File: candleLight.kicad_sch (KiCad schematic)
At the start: 42 parts, among them J1 USB_C_Receptacle_USB2.0, J2 Conn_Phoenix, J3 Conn_SWD, J4 Conn_USART1, J5 Conn_BOOT0, SW1 MST22D18G2 125, U1 STM32F072C8Tx, U2 AMS1117-3.3, U3 TJA1051TK-3, Y1 8MHz

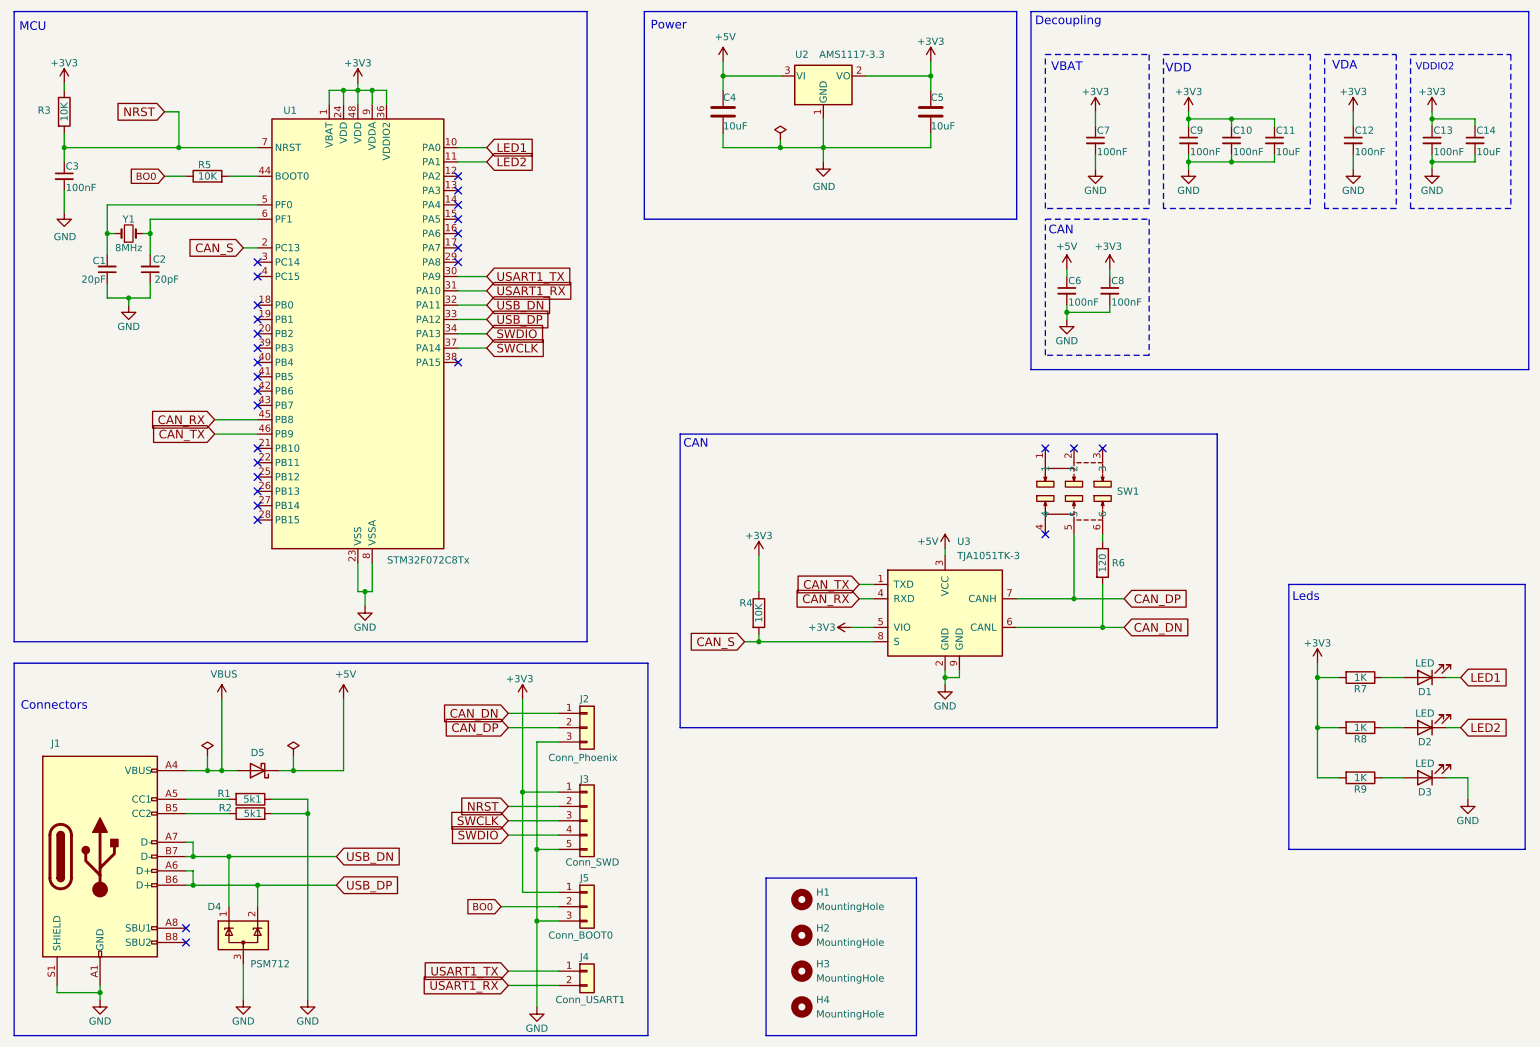
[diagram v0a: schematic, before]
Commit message: uppdate silkscreen and SPI header
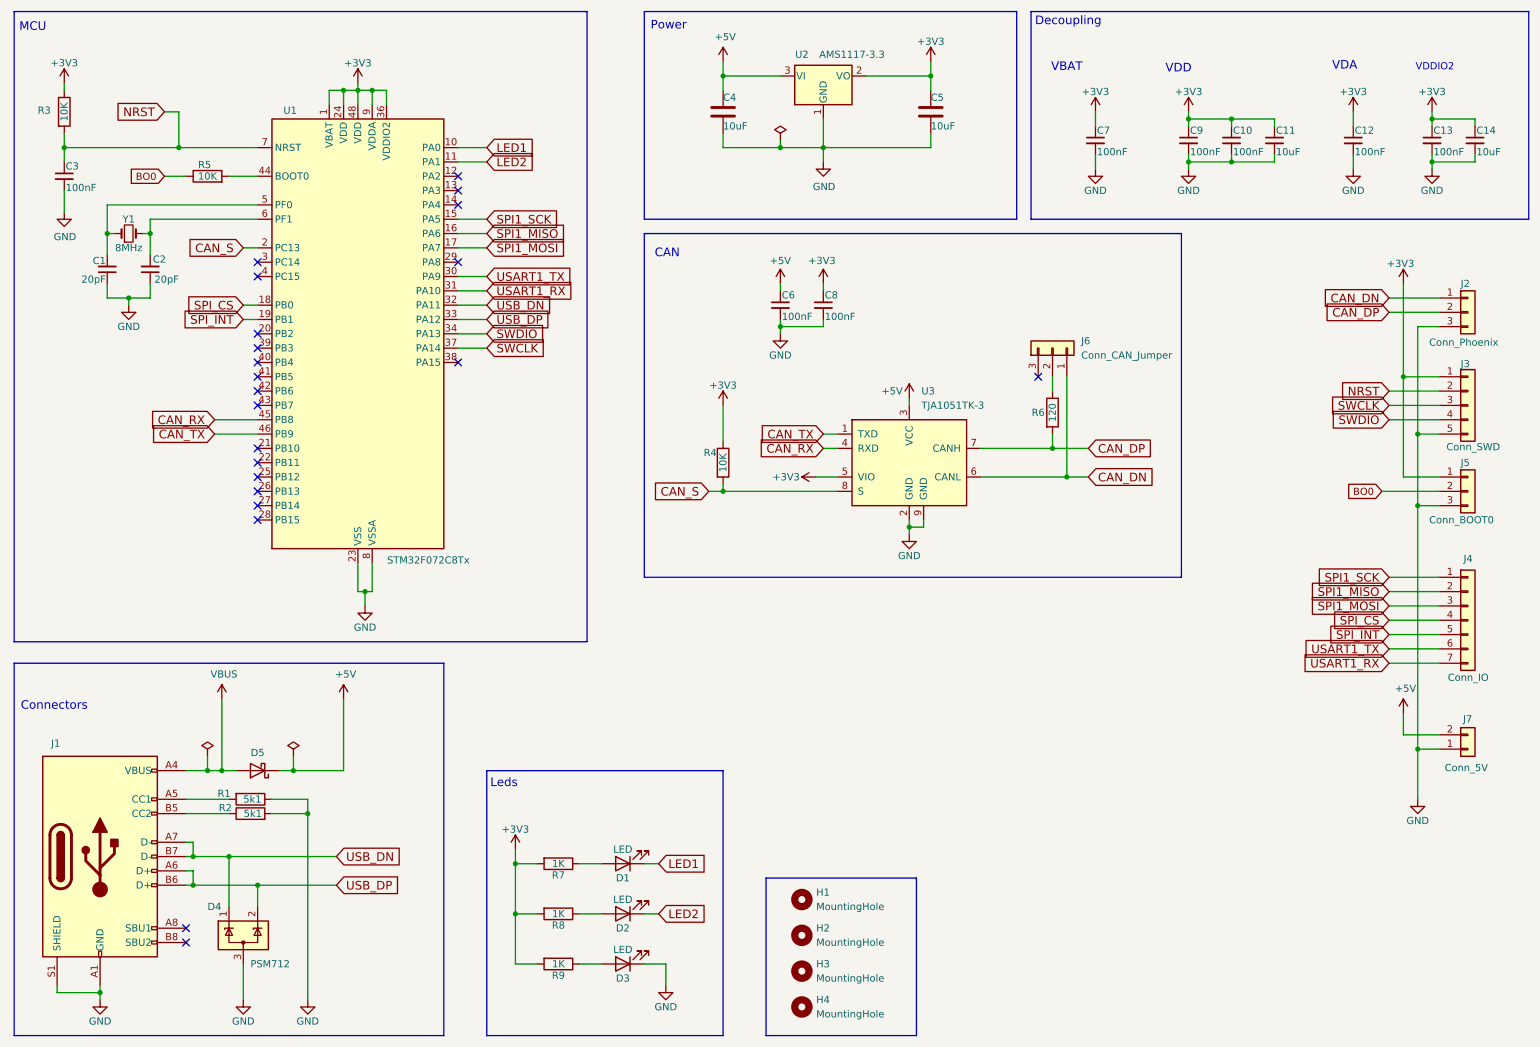
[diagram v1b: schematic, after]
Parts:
- removed J4: Conn_USART1, Connector_PinHeader_2.54mm:PinHeader_1x02_P2.54mm_Vertical, symbol Connector_Generic:Conn_01x02
- removed SW1: MST22D18G2 125, woldhack:SW-SMD_MST22D18G2, symbol woldhack:MST22D18G2125
- added J4: Conn_IO, Connector_PinHeader_2.54mm:PinHeader_1x07_P2.54mm_Vertical, symbol Connector_Generic:Conn_01x07
- added J6: Conn_CAN_Jumper, Connector_PinHeader_2.54mm:PinHeader_1x03_P2.54mm_Vertical, symbol Connector_Generic:Conn_01x03
- added J7: Conn_5V, Connector_PinHeader_2.54mm:PinHeader_1x02_P2.54mm_Vertical, symbol Connector_Generic:Conn_01x02
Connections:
- net +5V: now also J7.2 (Pin_1)
- net CAN_DN: now also J6.1 (Pin_3); no longer R6.2
- net CAN_DP: now also R6.2
- net GND: now also J7.1 (Pin_2)
- net USART1_RX: now also J4.7 (Pin_7)
- net USART1_TX: now also J4.6 (Pin_6)
- net at R6.1: now also J6.2 (Pin_2)
- net SPI1_SCK: now reaches U1.15 (PA5)
- net SPI1_SCK: now also J4.1 (Pin_1)
- net SPI1_MISO: now reaches U1.16 (PA6)
- net SPI1_MISO: now also J4.2 (Pin_2)
- net SPI1_MOSI: now reaches U1.17 (PA7)
- net SPI1_MOSI: now also J4.3 (Pin_3)
- net SPI_CS: now reaches U1.18 (PB0)
- net SPI_CS: now also J4.4 (Pin_4)
- net SPI_INT: now reaches U1.19 (PB1)
- net SPI_INT: now also J4.5 (Pin_5)
- no-connect marks 30 -> 22
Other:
- moved on the sheet: C6, C8, D1, D2, D3, J2, J3, J5, R4, R6, R7, R8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

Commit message: production
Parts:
- C1, C2: LCSC C1554 -> C1648
- C11, C14: LCSC C440198 -> C15850
- C4, C5: value C_10UF_0805 -> 10uF; Display 10uF -> (none)
- J2: LCSC (none) -> C474951
- J3: LCSC (none) -> C32713271
- J4: LCSC (none) -> C32713273
- J5, J6: LCSC (none) -> C32713269
- U3: LCSC (none) -> C2875699
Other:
- moved on the sheet: J5
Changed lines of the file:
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@@
 	)
 	(junction
+		(at 262.89 102.87)
+		(diameter 0)
+		(color 0 0 0 0)
+	)
+	(junction
 		(at 57.15 168.91)
 		(diameter 0)
@@
 	)
 	(junction
-		(at 262.89 101.6)
-		(diameter 0)
-		(color 0 0 0 0)
-	)
-	(junction
 		(at 102.87 173.99)
 		(diameter 0)
@@
 	(wire
 		(pts
-			(xy 260.35 96.52) (xy 260.35 78.74)
+			(xy 260.35 97.79) (xy 260.35 78.74)
 		)
 		(stroke
@@
 	(wire
 		(pts
-			(xy 262.89 101.6) (xy 262.89 144.78)
+			(xy 262.89 88.9) (xy 262.89 102.87)
 		)
 		(stroke
@@
 	(wire
 		(pts
+			(xy 262.89 102.87) (xy 262.89 144.78)
+		)
+		(stroke
+			(width 0)
+			(type default)
+		)
+	)
+	(wire
+		(pts
 			(xy 237.49 33.02) (xy 237.49 34.29)
 		)
@@
 	(wire
 		(pts
-			(xy 262.89 88.9) (xy 262.89 101.6)
-		)
-		(stroke
-			(width 0)
-			(type default)
-		)
-	)
-	(wire
-		(pts
 			(xy 157.48 33.02) (xy 157.48 38.1)
 		)
@@
 	(wire
 		(pts
-			(xy 260.35 96.52) (xy 266.7 96.52)
+			(xy 260.35 97.79) (xy 266.7 97.79)
 		)
 		(stroke
@@
 	(wire
 		(pts
-			(xy 262.89 101.6) (xy 266.7 101.6)
+			(xy 262.89 102.87) (xy 266.7 102.87)
 		)
 		(stroke
@@
 	(wire
 		(pts
-			(xy 256.54 99.06) (xy 266.7 99.06)
-		)
-		(stroke
-			(width 0)
-			(type default)
-		)
-	)
-	(wire
-		(pts
 			(xy 44.45 163.83) (xy 45.72 163.83)
 		)
@@
 	(wire
 		(pts
+			(xy 256.54 100.33) (xy 266.7 100.33)
+		)
+		(stroke
+			(width 0)
+			(type default)
+		)
+	)
+	(wire
+		(pts
 			(xy 198.12 88.9) (xy 198.12 91.44)
 		)
@@
 	(global_label "BO0"
 		(shape input)
-		(at 256.54 99.06 180)
+		(at 256.54 100.33 180)
 		(fields_autoplaced yes)
 		(effects
@@
 		)
 		(property "Intersheetrefs" "${INTERSHEET_REFS}"
-			(at 250.399 99.06 0)
+			(at 250.399 100.33 0)
 			(effects
 				(font
@@
 	(symbol
 		(lib_id "Connector_Generic:Conn_01x03")
-		(at 271.78 99.06 0)
+		(at 271.78 100.33 0)
 		(unit 1)
 		(exclude_from_sim no)
@@
 		(dnp no)
 		(property "Reference" "J5"
-			(at 270.51 93.98 0)
+			(at 270.51 95.25 0)
 			(effects
 				(font
@@
 		)
 		(property "Value" "Conn_BOOT0"
-			(at 264.922 104.14 0)
+			(at 264.922 105.41 0)
 			(effects
 				(font
@@
 		)
 		(property "Footprint" "Connector_PinHeader_2.54mm:PinHeader_1x03_P2.54mm_Vertical"
-			(at 271.78 99.06 0)
+			(at 271.78 100.33 0)
 			(effects
 				(font
@@
 		)
 		(property "Datasheet" "~"
-			(at 271.78 99.06 0)
+			(at 271.78 100.33 0)
 			(effects
 				(font
@@
 		)
 		(property "Description" "Generic connector, single row, 01x03, script generated (kicad-library-utils/schlib/autogen/connector/)"
-			(at 271.78 99.06 0)
+			(at 271.78 100.33 0)
 			(effects
 				(font
@@
 			)
 		)
+		(property "LCSC" "C32713269"
+			(at 271.78 100.33 0)
+			(effects
+				(font
+					(size 1.524 1.524)
+				)
+				(hide yes)
+			)
+		)
 		(pin "3"
 		)
@@
 			)
 		)
+		(property "LCSC" "C32713273"
+			(at 271.78 121.92 0)
+			(effects
+				(font
+					(size 1.524 1.524)
+				)
+				(hide yes)
+			)
+		)
 		(pin "1"
 		)
@@
 			)
 		)
+		(property "LCSC" "C2875699"
+			(at 172.72 93.98 0)
+			(effects
+				(font
+					(size 1.524 1.524)
+				)
+				(hide yes)
+			)
+		)
 		(pin "4"
 		)
@@
 			)
 		)
-		(property "LCSC" "C1554"
+		(property "LCSC" "C1648"
 			(at 30.48 59.69 90)
 			(effects
@@
 			)
 		)
-		(property "LCSC" "C1554"
+		(property "LCSC" "C1648"
 			(at 38.1 59.69 90)
 			(effects
@@
 			)
 		)
-		(property "Value" "C_10UF_0805"
-			(at 140.97 35.56 0)
+		(property "Value" "10uF"
+			(at 140.462 34.036 0)
 			(effects
 				(font
@@
 				)
 				(justify left)
-				(hide yes)
 			)
 		)
@@
 					(size 1.27 1.27)
 				)
-			)
-		)
-		(property "Display" "10uF"
-			(at 139.7 34.29 0)
-			(effects
-				(font
-					(size 1.27 1.27)
-				)
-				(justify left)
+				(hide yes)
 			)
 		)
@@
 			)
 		)
-		(property "LCSC" ""
+		(property "LCSC" "C474951"
 			(at 271.78 67.31 0)
 			(effects
@@
 					(size 1.27 1.27)
 				)
+				(hide yes)
 			)
 		)
@@
 			)
 		)
+		(property "LCSC" "C32713271"
+			(at 271.78 83.82 0)
+			(effects
+				(font
+					(size 1.524 1.524)
+				)
+				(hide yes)
+			)
+		)
 		(pin "1"
 		)
@@
 			)
 		)
-		(property "LCSC" "C440198"
+		(property "LCSC" "C15850"
 			(at 237.49 36.83 0)
 			(effects
@@
 			)
 		)
-		(property "LCSC" "C440198"
+		(property "LCSC" "C15850"
 			(at 273.05 36.83 0)
 			(effects
@@
 			)
 		)
+		(property "LCSC" "C32713269"
+			(at 198.12 73.66 90)
+			(effects
+				(font
+					(size 1.524 1.524)
+				)
+				(hide yes)
+			)
+		)
 		(pin "2"
 		)
@@
 			)
 		)
-		(property "Value" "C_10UF_0805"
-			(at 177.8 35.56 0)
+		(property "Value" "10uF"
+			(at 177.292 34.544 0)
 			(effects
 				(font
@@
 				)
 				(justify left)
-				(hide yes)
 			)
 		)
@@
 			)
 		)
-		(property "Display" "10uF"
-			(at 176.53 34.29 0)
-			(effects
-				(font
-					(size 1.27 1.27)
-				)
-				(justify left)
-			)
-		)

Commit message: update load caps
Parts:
- C1, C2: value 20pF -> 30pF; LCSC C1648 -> C1658
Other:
- company: (none) -> woldhack
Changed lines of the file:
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@@
 		(title "canleLight")
 		(date "2025-10-05")
-		(rev "V2")
+		(rev "V2.1")
+		(company "woldhack")
 	)
 	(rectangle
@@
 			)
 		)
-		(property "Value" "20pF"
+		(property "Value" "30pF"
 			(at 30.226 61.468 0)
 			(effects
@@
 			)
 		)
-		(property "LCSC" "C1648"
+		(property "LCSC" "C1658"
 			(at 30.48 59.69 90)
 			(effects
@@
 			)
 		)
-		(property "Value" "20pF"
+		(property "Value" "30pF"
 			(at 43.18 61.468 0)
 			(effects
@@
 			)
 		)
-		(property "LCSC" "C1648"
+		(property "LCSC" "C1658"
 			(at 38.1 59.69 90)
 			(effects
